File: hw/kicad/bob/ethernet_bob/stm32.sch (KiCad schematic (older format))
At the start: 22 parts, among them P1 USB_OTG, P2 CONN_02X25, P3 CONN_02X25, SW1 SW_PUSH, U2 STM32F407VETx, X1 CRYSTAL_SMD

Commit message: add rmii testpoints
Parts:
- added W1, W10, W11, W2, W3, W4, W5, W6, W7, W8, W9: TEST_1P, Wire_Pads:SolderWirePad_single_0-8mmDrill, symbol TEST_1P
- gave numbers to parts that had none: 3
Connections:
- net STM_MCO1: now also W8.1
- net STM_MDC: now also W3.1
- net STM_RXD0: now also W2.1
- net STM_RXD1: now also W1.1
- net STM_RXDV: now also W9.1
- net STM_RXER: now also W7.1
- net STM_TXD0: now also W5.1
- net STM_TXD1: now also W4.1
- net STM_TXEN: now also W6.1
- net PA11: now reaches U2.70 (ADC1_EXTI11/ADC2_EXTI11/ADC3_EXTI11/CAN1_RX/TIM1_CH4/USART1_CTS/USB_OTG_FS_DM/PA11)
- net PA11: now also W10.1
- net PA12: now reaches U2.71 (CAN1_TX/TIM1_ETR/USART1_RTS/USB_OTG_FS_DP/PA12)
- net PA12: now also W11.1
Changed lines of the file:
@@
 	11850 2050 11950 2050
 $Comp
-L C C?
+L C C19
 U 1 1 57ED55B5
 P 1200 2050
-F 0 "C?" H 1085 2004 50  0000 R CNN
+F 0 "C19" H 1085 2004 50  0000 R CNN
 F 1 "100n" H 1085 2095 50  0000 R CNN
 F 2 "Capacitors_SMD:C_0603" H 1238 1900 50  0001 C CNN
@@
 $EndComp
 $Comp
-L C C?
+L C C18
 U 1 1 57ED57EF
 P 1000 2050
-F 0 "C?" H 885 2004 50  0000 R CNN
+F 0 "C18" H 885 2004 50  0000 R CNN
 F 1 "100n" H 885 2095 50  0000 R CNN
 F 2 "Capacitors_SMD:C_0603" H 1038 1900 50  0001 C CNN
@@
 	750  2200 1200 2200
 $Comp
-L GND #PWR?
+L GND #PWR028
 U 1 1 57ED5C25
 P 1100 2200
-F 0 "#PWR?" H 1100 1950 50  0001 C CNN
+F 0 "#PWR028" H 1100 1950 50  0001 C CNN
 F 1 "GND" H 1105 2027 50  0000 C CNN
 F 2 "" H 1100 2200 50  0000 C CNN
@@
 $EndComp
 $Comp
-L +3.3V #PWR?
+L +3.3V #PWR029
 U 1 1 57ED5D80
 P 1150 1600
-F 0 "#PWR?" H 1150 1450 50  0001 C CNN
+F 0 "#PWR029" H 1150 1450 50  0001 C CNN
 F 1 "+3.3V" H 1165 1773 50  0000 C CNN
 F 2 "" H 1150 1600 50  0000 C CNN
@@
 Connection ~ 1250 1600
 $Comp
-L C C?
+L C C17
 U 1 1 57ED64E7
 P 750 2050
-F 0 "C?" H 635 2004 50  0000 R CNN
+F 0 "C17" H 635 2004 50  0000 R CNN
 F 1 "100n" H 635 2095 50  0000 R CNN
 F 2 "Capacitors_SMD:C_0603" H 788 1900 50  0001 C CNN
@@
 	750  1900 750  1700
 Connection ~ 1250 1700
+$Comp
+L TEST_1P W3
+U 1 1 57ED6E33
+P 14350 7100
+F 0 "W3" H 14408 7220 50  0000 L CNN
+F 1 "TEST_1P" H 14408 7129 50  0000 L CNN
+F 2 "Wire_Pads:SolderWirePad_single_0-8mmDrill" H 14550 7100 50  0001 C CNN
+F 3 "" H 14550 7100 50  0000 C CNN
+	1    14350 7100
+	0    -1   -1   0
+$EndComp
+$Comp
+L TEST_1P W2
+U 1 1 57ED6ED0
+P 14350 7000
+F 0 "W2" H 14408 7120 50  0000 L CNN
+F 1 "TEST_1P" H 14408 7029 50  0000 L CNN
+F 2 "Wire_Pads:SolderWirePad_single_0-8mmDrill" H 14550 7000 50  0001 C CNN
+F 3 "" H 14550 7000 50  0000 C CNN
+	1    14350 7000
+	0    -1   -1   0
+$EndComp
+$Comp
+L TEST_1P W1
+U 1 1 57ED6F40
+P 14350 6900
+F 0 "W1" H 14408 7020 50  0000 L CNN
+F 1 "TEST_1P" H 14408 6929 50  0000 L CNN
+F 2 "Wire_Pads:SolderWirePad_single_0-8mmDrill" H 14550 6900 50  0001 C CNN
+F 3 "" H 14550 6900 50  0000 C CNN
+	1    14350 6900
+	0    -1   -1   0
+$EndComp
+$Comp
+L TEST_1P W11
+U 1 1 57ED7269
+P 14350 7900
+F 0 "W11" H 14408 8020 50  0000 L CNN
+F 1 "TEST_1P" H 14408 7929 50  0000 L CNN
+F 2 "Wire_Pads:SolderWirePad_single_0-8mmDrill" H 14550 7900 50  0001 C CNN
+F 3 "" H 14550 7900 50  0000 C CNN
+	1    14350 7900
+	0    -1   -1   0
+$EndComp
+$Comp
+L TEST_1P W10
+U 1 1 57ED726F
+P 14350 7800
+F 0 "W10" H 14408 7920 50  0000 L CNN
+F 1 "TEST_1P" H 14408 7829 50  0000 L CNN
+F 2 "Wire_Pads:SolderWirePad_single_0-8mmDrill" H 14550 7800 50  0001 C CNN
+F 3 "" H 14550 7800 50  0000 C CNN
+	1    14350 7800
+	0    -1   -1   0
+$EndComp
+$Comp
+L TEST_1P W7
+U 1 1 57ED7275
+P 14350 7500
+F 0 "W7" H 14408 7620 50  0000 L CNN
+F 1 "TEST_1P" H 14408 7529 50  0000 L CNN
+F 2 "Wire_Pads:SolderWirePad_single_0-8mmDrill" H 14550 7500 50  0001 C CNN
+F 3 "" H 14550 7500 50  0000 C CNN
+	1    14350 7500
+	0    -1   -1   0
+$EndComp
+$Comp
+L TEST_1P W6
+U 1 1 57ED727B
+P 14350 7400
+F 0 "W6" H 14408 7520 50  0000 L CNN
+F 1 "TEST_1P" H 14408 7429 50  0000 L CNN
+F 2 "Wire_Pads:SolderWirePad_single_0-8mmDrill" H 14550 7400 50  0001 C CNN
+F 3 "" H 14550 7400 50  0000 C CNN
+	1    14350 7400
+	0    -1   -1   0
+$EndComp
+$Comp
+L TEST_1P W5
+U 1 1 57ED7281
+P 14350 7300
+F 0 "W5" H 14408 7420 50  0000 L CNN
+F 1 "TEST_1P" H 14408 7329 50  0000 L CNN
+F 2 "Wire_Pads:SolderWirePad_single_0-8mmDrill" H 14550 7300 50  0001 C CNN
+F 3 "" H 14550 7300 50  0000 C CNN
+	1    14350 7300
+	0    -1   -1   0
+$EndComp
+$Comp
+L TEST_1P W4
+U 1 1 57ED7287
+P 14350 7200
+F 0 "W4" H 14408 7320 50  0000 L CNN
+F 1 "TEST_1P" H 14408 7229 50  0000 L CNN
+F 2 "Wire_Pads:SolderWirePad_single_0-8mmDrill" H 14550 7200 50  0001 C CNN
+F 3 "" H 14550 7200 50  0000 C CNN
+	1    14350 7200
+	0    -1   -1   0
+$EndComp
+Text HLabel 14450 7700 2    60   Input ~ 0
+STM_RXDV
+Text HLabel 14450 7600 2    60   Input ~ 0
+STM_MCO1
+Text HLabel 14450 7500 2    60   Input ~ 0
+STM_RXER
+Text HLabel 14450 7400 2    60   Input ~ 0
+STM_TXEN
+Text HLabel 14450 7300 2    60   Input ~ 0
+STM_TXD0
+Text HLabel 14450 7200 2    60   Input ~ 0
+STM_TXD1
+Text HLabel 14450 7100 2    60   Input ~ 0
+STM_MDC
+Text HLabel 14450 7000 2    60   Input ~ 0
+STM_RXD0
+Text HLabel 14450 6900 2    60   Input ~ 0
+STM_RXD1
+Wire Wire Line
+	14450 7700 14350 7700
+Wire Wire Line
+	14450 7600 14350 7600
+Wire Wire Line
+	14450 7500 14350 7500
+Wire Wire Line
+	14450 7400 14350 7400
+Wire Wire Line
+	14450 7300 14350 7300
+Wire Wire Line
+	14450 7200 14350 7200
+Wire Wire Line
+	14450 7100 14350 7100
+Wire Wire Line
+	14450 7000 14350 7000
+Wire Wire Line
+	14450 6900 14350 6900
+Text GLabel 10400 2300 2    60   Input ~ 0
+PA11
+Text GLabel 10400 2400 2    60   Input ~ 0
+PA12
+Wire Wire Line
+	10300 2300 10400 2300
+Wire Wire Line
+	10300 2400 10400 2400
+$Comp
+L TEST_1P W9
+U 1 1 57EDA436
+P 14350 7700
+F 0 "W9" H 14408 7820 50  0000 L CNN
+F 1 "TEST_1P" H 14408 7729 50  0000 L CNN
+F 2 "Wire_Pads:SolderWirePad_single_0-8mmDrill" H 14550 7700 50  0001 C CNN
+F 3 "" H 14550 7700 50  0000 C CNN
+	1    14350 7700
+	0    -1   -1   0
+$EndComp
+$Comp
+L TEST_1P W8
+U 1 1 57EDA43C
+P 14350 7600
+F 0 "W8" H 14408 7720 50  0000 L CNN
+F 1 "TEST_1P" H 14408 7629 50  0000 L CNN
+F 2 "Wire_Pads:SolderWirePad_single_0-8mmDrill" H 14550 7600 50  0001 C CNN
+F 3 "" H 14550 7600 50  0000 C CNN
+	1    14350 7600
+	0    -1   -1   0
+$EndComp
+Text GLabel 14450 7800 2    60   Input ~ 0
+PA11
+Text GLabel 14450 7900 2    60   Input ~ 0
+PA12
+Wire Wire Line
+	14350 7800 14450 7800
+Wire Wire Line
+	14350 7900 14450 7900
 $EndSCHEMATC

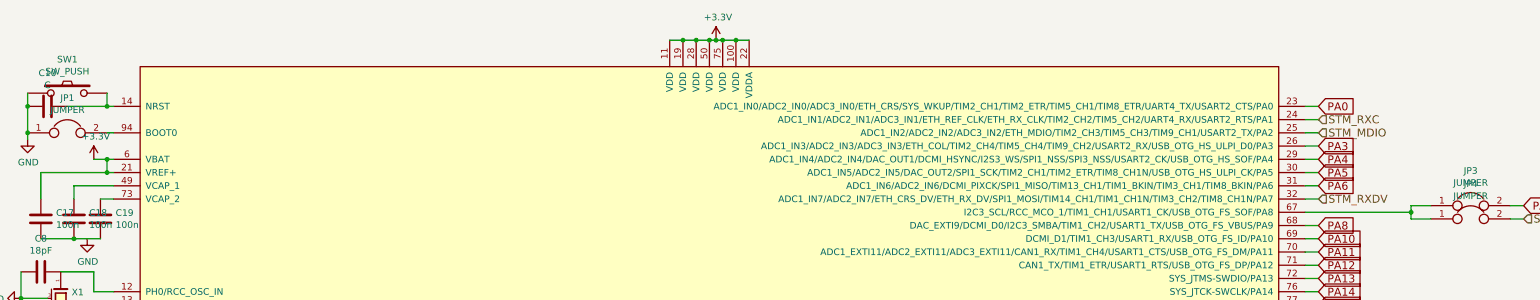
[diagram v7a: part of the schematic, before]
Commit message: change phy schematic
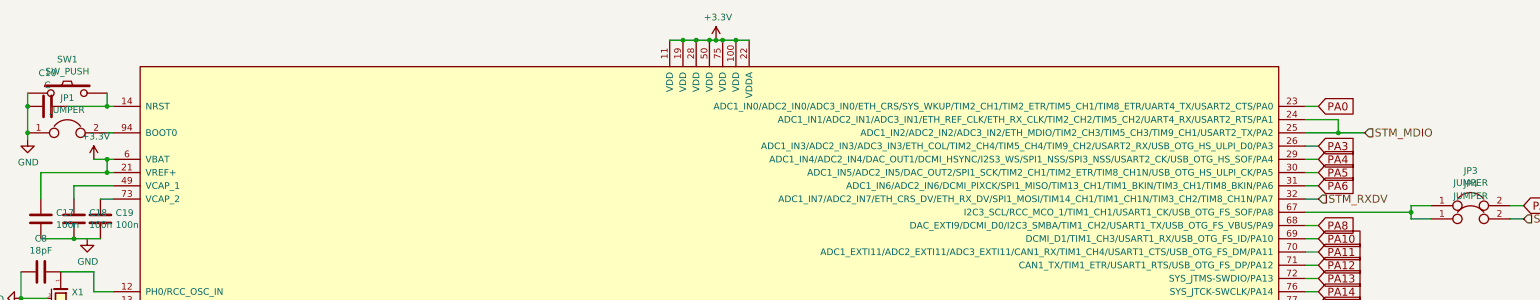
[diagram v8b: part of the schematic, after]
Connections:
- net STM_RXC is gone; now on net STM_MDIO: U2.24 (ADC1_IN1/ADC2_IN1/ADC3_IN1/ETH_REF_CLK/ETH_RX_CLK/TIM2_CH2/TIM5_CH2/UART4_RX/USART2_RTS/PA1)
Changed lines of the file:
@@
 EESchema Schematic File Version 2
-LIBS:power
-LIBS:device
-LIBS:transistors
-LIBS:conn
-LIBS:linear
-LIBS:regul
-LIBS:74xx
-LIBS:cmos4000
-LIBS:adc-dac
-LIBS:memory
-LIBS:xilinx
-LIBS:microcontrollers
-LIBS:dsp
-LIBS:microchip
-LIBS:analog_switches
-LIBS:motorola
-LIBS:texas
-LIBS:intel
-LIBS:audio
-LIBS:interface
-LIBS:digital-audio
-LIBS:philips
-LIBS:display
-LIBS:cypress
-LIBS:siliconi
-LIBS:opto
-LIBS:atmel
-LIBS:contrib
-LIBS:valves
+LIBS:ethernet_bob-rescue
 LIBS:ksz8081
-LIBS:ESD_Protection
 LIBS:hr911105_rj45
-LIBS:stm32
 LIBS:ethernet_bob-cache
 EELAYER 25 0
@@
 Text HLabel 10400 1900 2    60   Input ~ 0
 STM_RXDV
-Text HLabel 10400 1400 2    60   Input ~ 0
+Text HLabel 10750 1400 2    60   Input ~ 0
 STM_MDIO
 Text HLabel 11000 4000 2    60   Input ~ 0
@@
 	1    0    0    -1
 $EndComp
-Text HLabel 10400 1300 2    60   Input ~ 0
-STM_RXC
 $Comp
 L +5VP #PWR06
@@
 	10300 1200 10400 1200
 Wire Wire Line
-	10300 1400 10400 1400
+	10300 1400 10750 1400
 Wire Wire Line
 	10300 1500 10400 1500
@@
 Connection ~ 650  1200
 Wire Wire Line
-	10300 1300 10400 1300
+	10300 1300 10550 1300
 Wire Wire Line
 	1600 7550 1700 7550
@@
 $EndComp
 Wire Wire Line
-	1300 1600 1150 1600
+	1150 1600 1300 1600
 Wire Wire Line
 	1250 1600 1250 1700
@@
 Wire Wire Line
 	14350 7900 14450 7900
+Wire Wire Line
+	10550 1300 10550 1400
+Connection ~ 10550 1400
 $EndSCHEMATC
